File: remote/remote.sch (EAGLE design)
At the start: 43 parts, among them IC1 ATMEGA168-MU, SW1 MF-SW-TACT-4.2MM, SW2 MF-SW-TACT-4.2MM, SW3 MF-SW-TACT-4.2MM, SW4 CT05-XXXX-J1, U2 NRF24L01SMD, Y1 16M, Y2 12MHz

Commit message: remote: drop unsused net
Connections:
- removed net XXX: IC1.PC2(ADC2/PCINT10)
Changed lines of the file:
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@@
-</segment>
-</net>
-<net name="XXX" class="0">
-<segment>
-<pinref part="IC1" gate="1" pin="PC2(ADC2/PCINT10)"/>
-<wire x1="104.14" y1="157.48" x2="114.3" y2="157.48" width="0.1524" layer="91"/>
-<label x="114.3" y="157.48" size="1.778" layer="95" rot="MR0"/>
 </segment>
 </net>

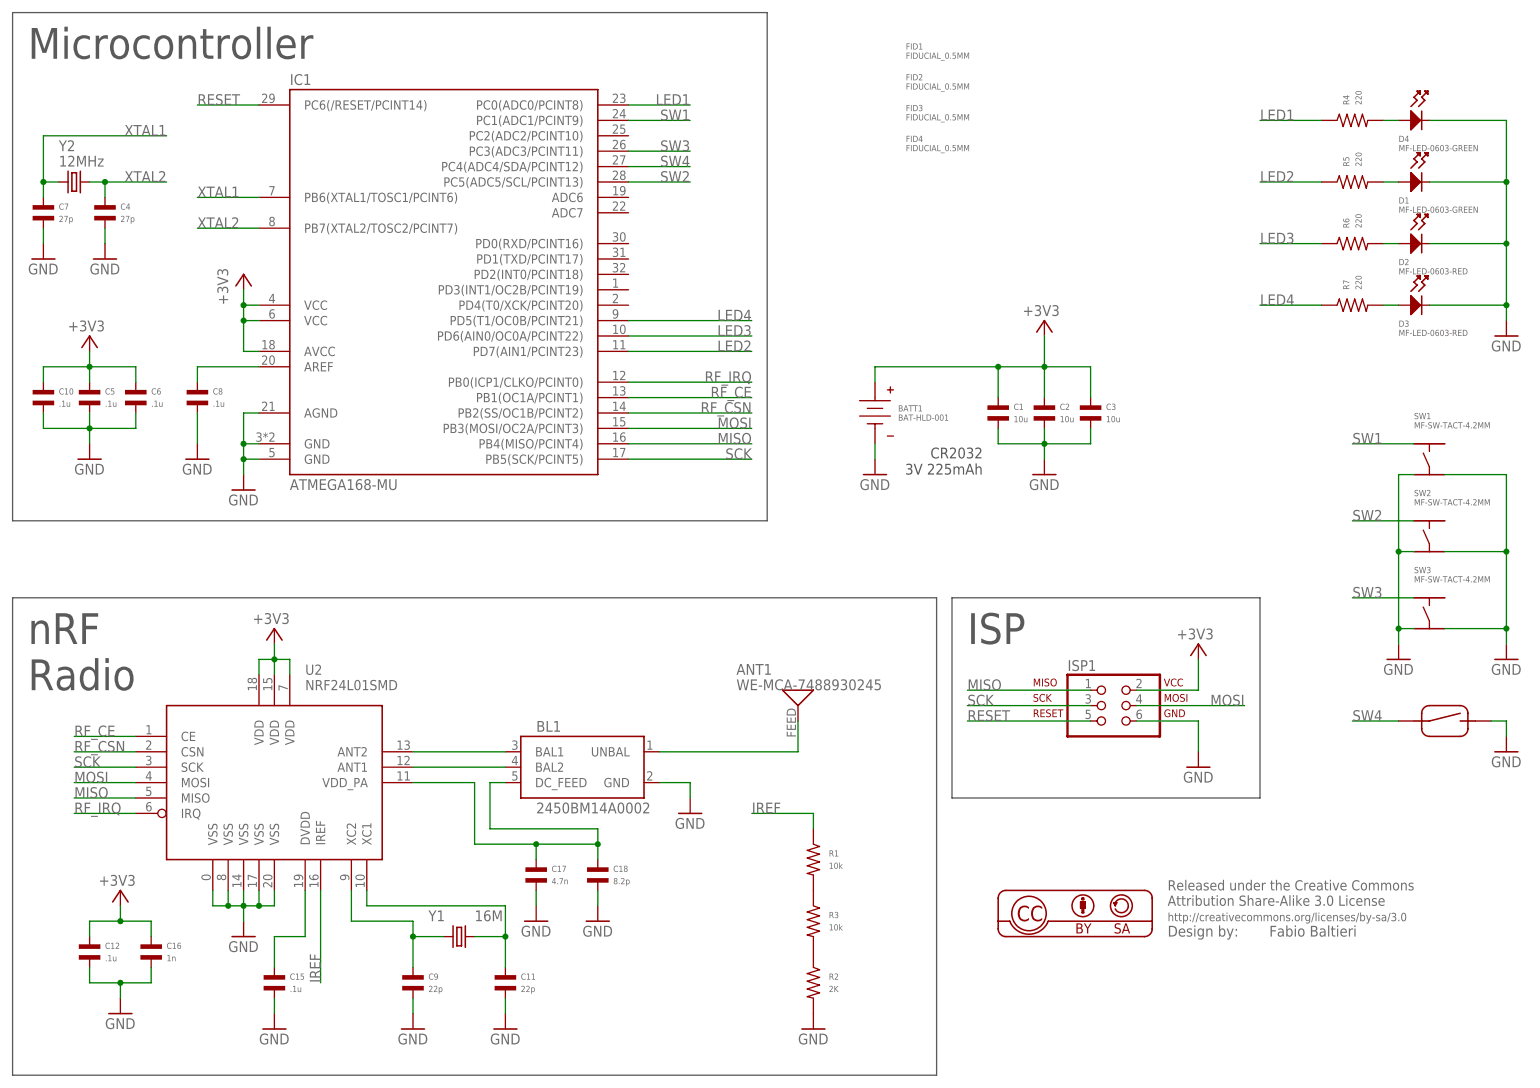
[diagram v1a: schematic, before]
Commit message: remote: schematics clean up
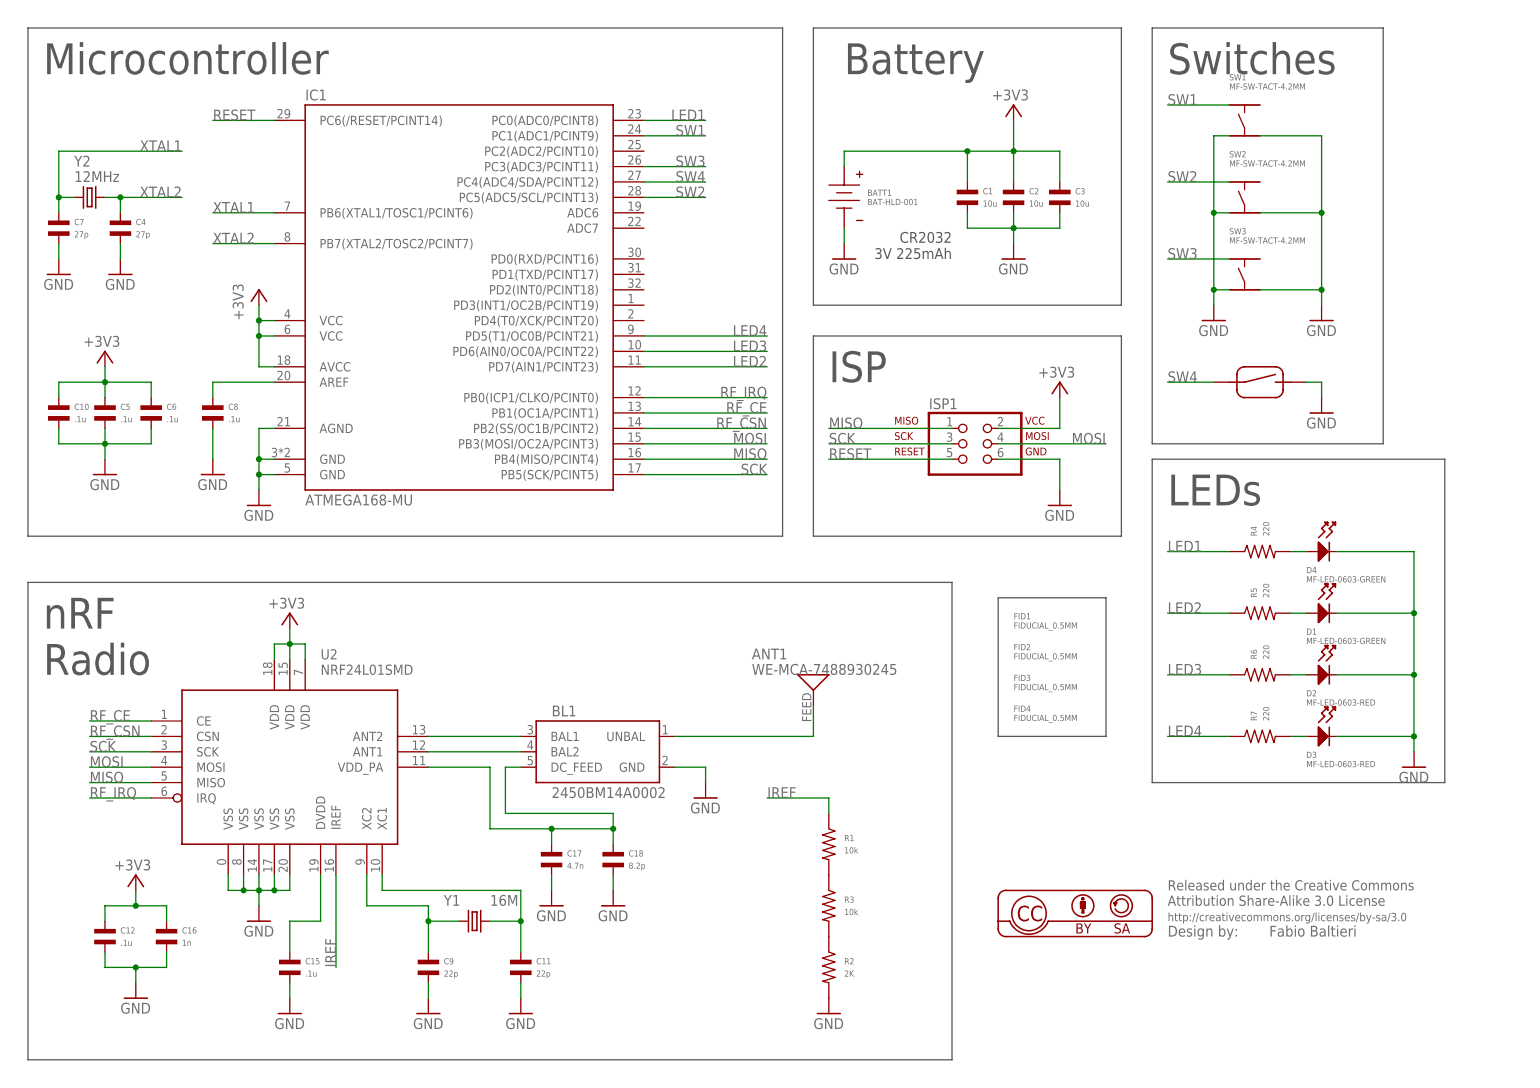
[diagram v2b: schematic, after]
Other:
- note added: "Battery"
- note added: "LEDs"
- note added: "Switches"
- moved on the sheet: ANT1, BATT1, BL1, C1, C10, C11, C12, C15, C16, C17, C18, C2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
